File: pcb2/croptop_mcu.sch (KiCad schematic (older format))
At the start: 63 parts, among them J1 USB-A1HSW6, J2 USB-A1HSW6, J3 68000-206HLF, SW1 SW_Push, U1 TPD4E1U06, U2 FSUSB42, U3 AP22802AW5, U4 AP22802AW5, U5 74AUP2G57, U6 PIC32MX795F512L, Y1 ABLS-8.000MHZ-B4-T

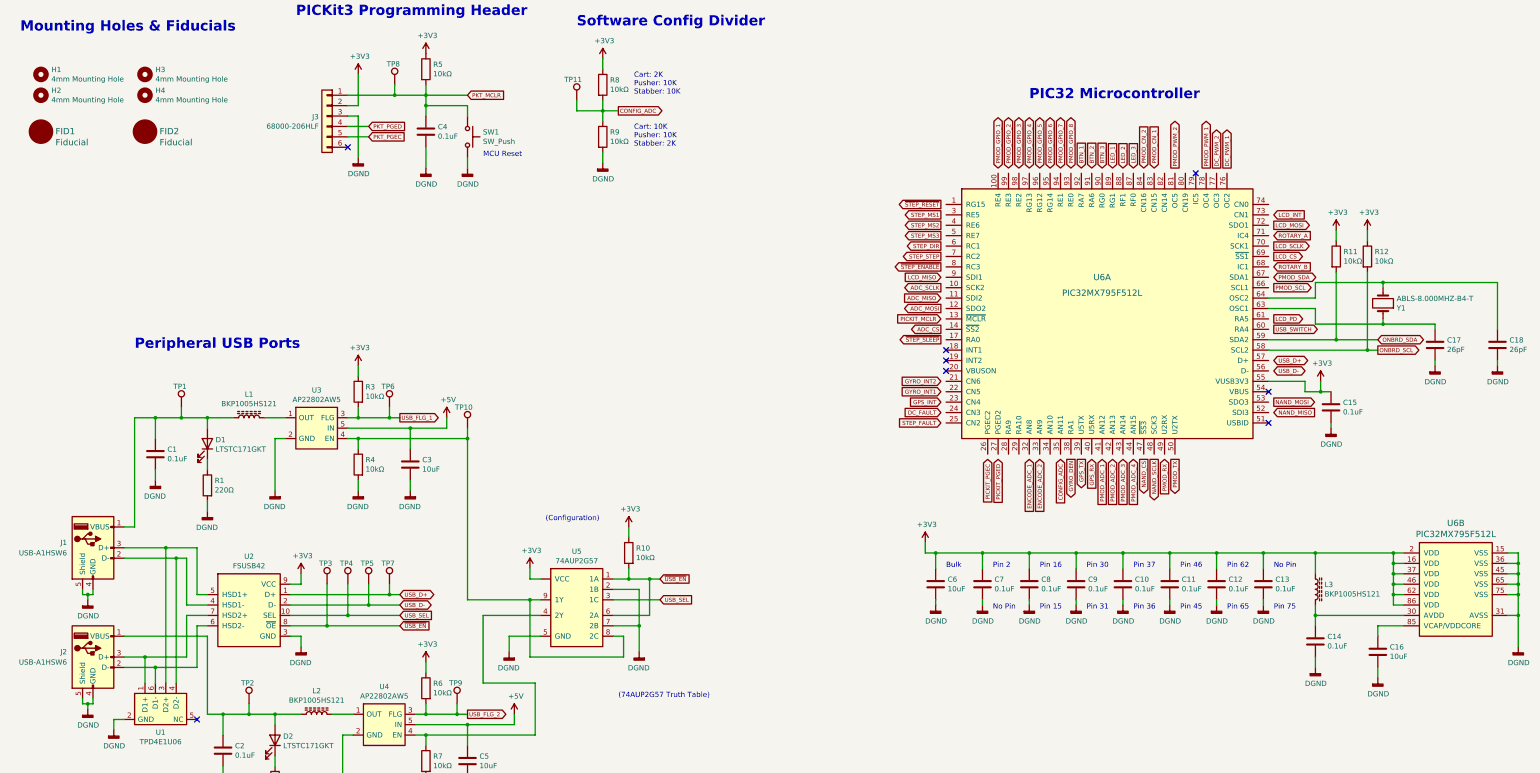
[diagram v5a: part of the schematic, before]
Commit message: Added TVS diodes
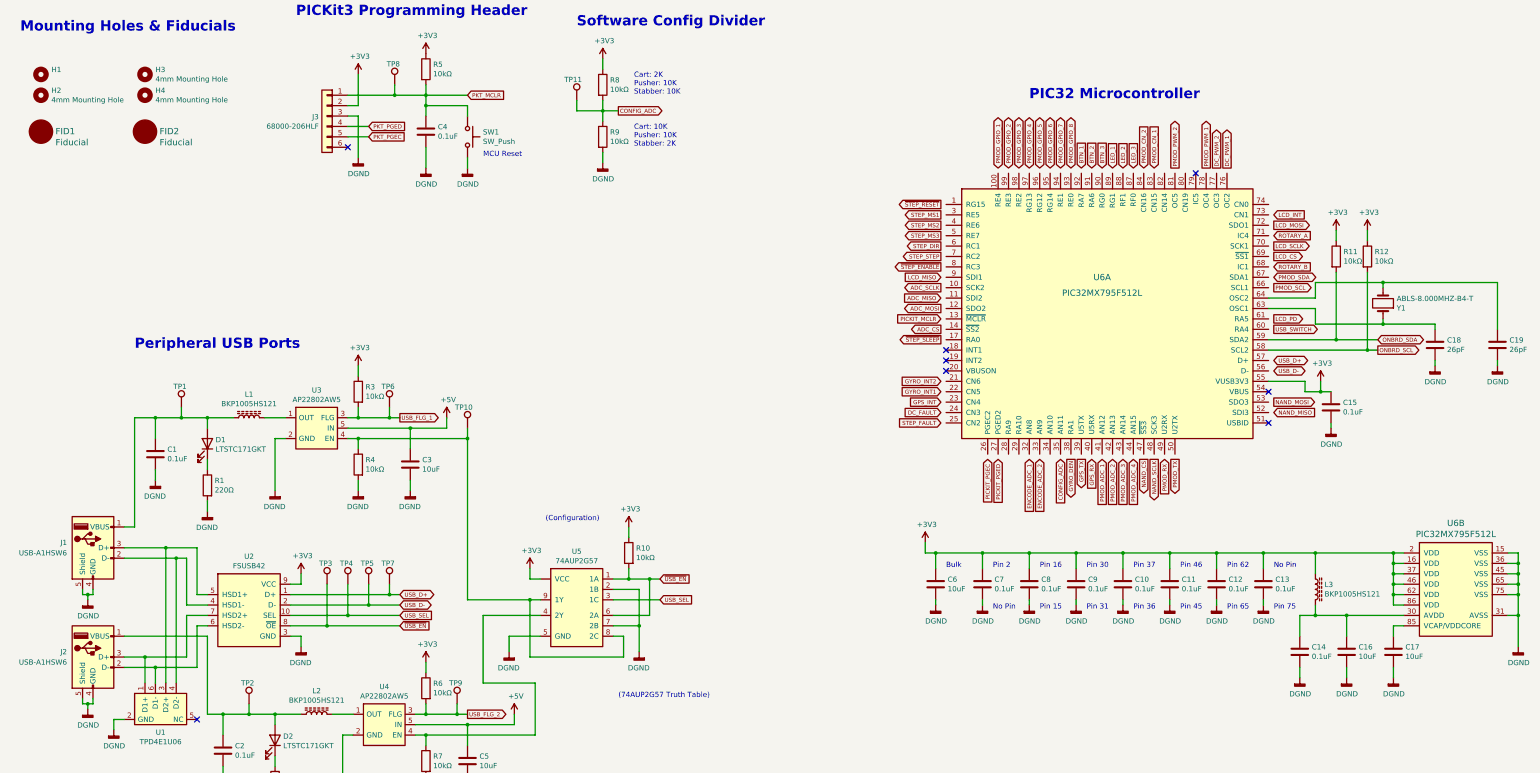
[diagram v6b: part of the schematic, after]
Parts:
- added C16: 10uF, Capacitor_SMD:C_0402_1005Metric, symbol Device:C
- renumbered C16 to C17, C17 to C18, C18 to C19
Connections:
- net DGND: now also C16.2
- net at C14.1, L3.2, U6.30 (AVDD): now also C16.1
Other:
- moved on the sheet: C14, C17
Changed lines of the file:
@@
 P 1200 1800
 F 0 "H1" H 1300 1846 50  0000 L CNN
-F 1 "4mm Mounting Hole" H 1300 1755 50  0000 L CNN
+F 1 "4mm Mounting Hole" H 1300 1755 50  0001 L CNN
 F 2 "MountingHole:MountingHole_4mm_Pad" H 1200 1800 50  0001 C CNN
 F 3 "" H 1200 1800 50  0001 C CNN
@@
 	14100 3800 14100 3850
 $Comp
-L CropTop:DGND #PWR047
+L CropTop:DGND #PWR048
 U 1 1 5D1D7CEB
 P 15200 4600
-F 0 "#PWR047" H 15200 4350 50  0001 C CNN
+F 0 "#PWR048" H 15200 4350 50  0001 C CNN
 F 1 "DGND" H 15204 4445 50  0000 C CNN
 F 2 "" H 15200 4600 50  0001 C CNN
@@
 $EndComp
 $Comp
-L CropTop:DGND #PWR046
+L CropTop:DGND #PWR047
 U 1 1 5D1D7CF1
 P 14600 4600
-F 0 "#PWR046" H 14600 4350 50  0001 C CNN
+F 0 "#PWR047" H 14600 4350 50  0001 C CNN
 F 1 "DGND" H 14604 4445 50  0000 C CNN
 F 2 "" H 14600 4600 50  0001 C CNN
@@
 P 15200 4400
 AR Path="/5D1D7CFB" Ref="C?"  Part="1"
-AR Path="/64807BBC/5D1D7CFB" Ref="C18"  Part="1"
-F 0 "C18" H 15315 4446 50  0000 L CNN
+AR Path="/64807BBC/5D1D7CFB" Ref="C19"  Part="1"
+F 0 "C19" H 15315 4446 50  0000 L CNN
 F 1 "26pF" H 15315 4355 50  0000 L CNN
 F 2 "Capacitor_SMD:C_0402_1005Metric" H 15238 4250 50  0001 C CNN
@@
 P 14600 4400
 AR Path="/5D1D7D02" Ref="C?"  Part="1"
-AR Path="/64807BBC/5D1D7D02" Ref="C17"  Part="1"
-F 0 "C17" H 14715 4446 50  0000 L CNN
+AR Path="/64807BBC/5D1D7D02" Ref="C18"  Part="1"
+F 0 "C18" H 14715 4446 50  0000 L CNN
 F 1 "26pF" H 14715 4355 50  0000 L CNN
 F 2 "Capacitor_SMD:C_0402_1005Metric" H 14638 4250 50  0001 C CNN
@@
 	14200 6400 14300 6400
 $Comp
-L CropTop:DGND #PWR048
+L CropTop:DGND #PWR049
 U 1 1 5D8970DB
 P 15400 7300
-F 0 "#PWR048" H 15400 7050 50  0001 C CNN
+F 0 "#PWR049" H 15400 7050 50  0001 C CNN
 F 1 "DGND" H 15404 7145 50  0000 C CNN
 F 2 "" H 15400 7300 50  0001 C CNN
@@
 	15400 6500 15400 6600
 $Comp
-L Device:C C16
+L Device:C C17
 U 1 1 5D939999
-P 14050 7350
-F 0 "C16" H 14165 7396 50  0000 L CNN
-F 1 "10uF" H 14165 7305 50  0000 L CNN
-F 2 "Capacitor_SMD:C_0402_1005Metric" H 14088 7200 50  0001 C CNN
-F 3 "" H 14050 7350 50  0001 C CNN
-	1    14050 7350
+P 14200 7350
+F 0 "C17" H 14315 7396 50  0000 L CNN
+F 1 "10uF" H 14315 7305 50  0000 L CNN
+F 2 "Capacitor_SMD:C_0402_1005Metric" H 14238 7200 50  0001 C CNN
+F 3 "" H 14200 7350 50  0001 C CNN
+	1    14200 7350
 	1    0    0    -1
 $EndComp
@@
 	1    0    0    -1
 $EndComp
-$Comp
-L CropTop:DGND #PWR03
-U 1 1 6104C614
-P 1900 8100
-AR Path="/64807BBC/6104C614" Ref="#PWR03"  Part="1"
-AR Path="/669AB112/6104C614" Ref="#PWR?"  Part="1"
-F 0 "#PWR03" H 1900 7850 50  0001 C CNN
-F 1 "DGND" H 1904 7945 50  0000 C CNN
-F 2 "" H 1900 8100 50  0001 C CNN
-F 3 "" H 1900 8100 50  0001 C CNN
-	1    1900 8100
-	1    0    0    -1
-$EndComp
-Wire Wire Line
-	2000 8000 1900 8000
-Wire Wire Line
-	1900 8000 1900 8100
 NoConn ~ 2700 8000
 NoConn ~ 13000 4850
@@
 Wire Wire Line
 	3700 7200 3700 7300
-$Comp
-L CropTop:TPD4E1U06 U?
-U 1 1 60F8235A
-P 2350 7900
-AR Path="/669AB112/60F8235A" Ref="U?"  Part="1"
-AR Path="/64807BBC/60F8235A" Ref="U1"  Part="1"
-F 0 "U1" H 2350 7676 50  0000 C CNN
-F 1 "TPD4E1U06" H 2350 7585 50  0000 C CNN
-F 2 "" V 2600 7350 50  0001 C CNN
-F 3 "" V 2600 7350 50  0001 C CNN
-	1    2350 7900
-	1    0    0    -1
-$EndComp
 Wire Wire Line
 	2600 7000 2600 7400
@@
 $EndComp
 $Comp
-L power:+3V3 #PWR044
+L power:+3V3 #PWR045
 U 1 1 5CF40AEC
 P 13950 3300
-F 0 "#PWR044" H 13950 3150 50  0001 C CNN
+F 0 "#PWR045" H 13950 3150 50  0001 C CNN
 F 1 "+3V3" H 13965 3473 50  0000 C CNN
 F 2 "" H 13950 3300 50  0001 C CNN
@@
 L Device:C C?
 U 1 1 5D054B37
-P 13450 7250
+P 13300 7350
 AR Path="/5D054B37" Ref="C?"  Part="1"
 AR Path="/66A12209/5D054B37" Ref="C?"  Part="1"
 AR Path="/64807BBC/5D054B37" Ref="C14"  Part="1"
-F 0 "C14" H 13565 7296 50  0000 L CNN
-F 1 "0.1uF" H 13565 7205 50  0000 L CNN
-F 2 "Capacitor_SMD:C_0402_1005Metric" H 13488 7100 50  0001 C CNN
-F 3 "" H 13450 7250 50  0001 C CNN
-	1    13450 7250
-	1    0    0    -1
-$EndComp
-$Comp
-L CropTop:DGND #PWR045
+F 0 "C14" H 13415 7396 50  0000 L CNN
+F 1 "0.1uF" H 13415 7305 50  0000 L CNN
+F 2 "Capacitor_SMD:C_0402_1005Metric" H 13338 7200 50  0001 C CNN
+F 3 "" H 13300 7350 50  0001 C CNN
+	1    13300 7350
+	1    0    0    -1
+$EndComp
+$Comp
+L CropTop:DGND #PWR046
 U 1 1 5D0824AF
-P 14050 7600
-F 0 "#PWR045" H 14050 7350 50  0001 C CNN
-F 1 "DGND" H 14054 7445 50  0000 C CNN
-F 2 "" H 14050 7600 50  0001 C CNN
-F 3 "" H 14050 7600 50  0001 C CNN
-	1    14050 7600
-	1    0    0    -1
-$EndComp
-Wire Wire Line
-	14050 7500 14050 7600
+P 14200 7600
+F 0 "#PWR046" H 14200 7350 50  0001 C CNN
+F 1 "DGND" H 14204 7445 50  0000 C CNN
+F 2 "" H 14200 7600 50  0001 C CNN
+F 3 "" H 14200 7600 50  0001 C CNN
+	1    14200 7600
+	1    0    0    -1
+$EndComp
+Wire Wire Line
+	14200 7500 14200 7600
 $Comp
 L CropTop:DGND #PWR040
 U 1 1 5D091954
-P 13450 7500
-F 0 "#PWR040" H 13450 7250 50  0001 C CNN
-F 1 "DGND" H 13454 7345 50  0000 C CNN
-F 2 "" H 13450 7500 50  0001 C CNN
-F 3 "" H 13450 7500 50  0001 C CNN
-	1    13450 7500
-	1    0    0    -1
-$EndComp
-Wire Wire Line
-	13450 7400 13450 7500
+P 13300 7600
+F 0 "#PWR040" H 13300 7350 50  0001 C CNN
+F 1 "DGND" H 13304 7445 50  0000 C CNN
+F 2 "" H 13300 7600 50  0001 C CNN
+F 3 "" H 13300 7600 50  0001 C CNN
+	1    13300 7600
+	1    0    0    -1
+$EndComp
+Wire Wire Line
+	13300 7500 13300 7600
 Wire Wire Line
 	12950 6400 13450 6400
@@
 	13450 6400 13450 6600
 Wire Wire Line
-	14050 7200 14050 7100
-Wire Wire Line
-	14050 7100 14300 7100
+	14200 7200 14200 7100
 Wire Wire Line
 	13450 6900 13450 7000
@@
 	13450 6400 14200 6400
 Connection ~ 13450 6400
-Wire Wire Line
-	13450 7000 14300 7000
-Connection ~ 13450 7000
-Wire Wire Line
-	13450 7000 13450 7100
 Connection ~ 2950 7950
 Connection ~ 3450 7950
@@
 Wire Wire Line
 	5950 7650 5950 8150
+$Comp
+L CropTop:TPD4E1U06 U?
+U 1 1 60F8235A
+P 2350 7900
+AR Path="/669AB112/60F8235A" Ref="U?"  Part="1"
+AR Path="/64807BBC/60F8235A" Ref="U1"  Part="1"
+F 0 "U1" H 2350 7676 50  0000 C CNN
+F 1 "TPD4E1U06" H 2350 7585 50  0000 C CNN
+F 2 "" V 2600 7350 50  0001 C CNN
+F 3 "" V 2600 7350 50  0001 C CNN
+	1    2350 7900
+	1    0    0    -1
+$EndComp
+Wire Wire Line
+	1900 8000 1900 8100
+Wire Wire Line
+	2000 8000 1900 8000
+$Comp
+L CropTop:DGND #PWR03
+U 1 1 6104C614
+P 1900 8100
+AR Path="/64807BBC/6104C614" Ref="#PWR03"  Part="1"
+AR Path="/669AB112/6104C614" Ref="#PWR?"  Part="1"
+F 0 "#PWR03" H 1900 7850 50  0001 C CNN
+F 1 "DGND" H 1904 7945 50  0000 C CNN
+F 2 "" H 1900 8100 50  0001 C CNN
+F 3 "" H 1900 8100 50  0001 C CNN
+	1    1900 8100
+	1    0    0    -1
+$EndComp
+$Comp
+L Device:C C16
+U 1 1 5DDFE105
+P 13750 7350
+F 0 "C16" H 13865 7396 50  0000 L CNN
+F 1 "10uF" H 13865 7305 50  0000 L CNN
+F 2 "Capacitor_SMD:C_0402_1005Metric" H 13788 7200 50  0001 C CNN
+F 3 "" H 13750 7350 50  0001 C CNN
+	1    13750 7350
+	1    0    0    -1
+$EndComp
+$Comp
+L CropTop:DGND #PWR044
+U 1 1 5DDFE10C
+P 13750 7600
+F 0 "#PWR044" H 13750 7350 50  0001 C CNN
+F 1 "DGND" H 13754 7445 50  0000 C CNN
+F 2 "" H 13750 7600 50  0001 C CNN
+F 3 "" H 13750 7600 50  0001 C CNN
+	1    13750 7600
+	1    0    0    -1
+$EndComp
+Wire Wire Line
+	13750 7500 13750 7600
+Wire Wire Line
+	14200 7100 14300 7100
+Wire Wire Line
+	13300 7000 13450 7000
+Wire Wire Line
+	13300 7000 13300 7200
+Connection ~ 13450 7000
+Wire Wire Line
+	13750 7200 13750 7000
+Wire Wire Line
+	13450 7000 13750 7000
+Connection ~ 13750 7000
+Wire Wire Line
+	13750 7000 14300 7000
 $EndSCHEMATC

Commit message: Updated pin out
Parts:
- removed C1, C10, C11, C12, C13, C14, C15, C2, C4, C7, C8, C9: 0.1uF, Capacitor_SMD:C_0402_1005Metric, symbol Device:C
- removed C16, C17, C3, C5, C6: 10uF, Capacitor_SMD:C_0402_1005Metric, symbol Device:C
- removed C18, C19: 26pF, Capacitor_SMD:C_0402_1005Metric, symbol Device:C
- removed D1, D2: LTSTC171GKT, LED_SMD:LED_0805_2012Metric, symbol Device:LED
- removed FID1, FID2: Fiducial, Fiducial:Fiducial_1mm_Dia_2.54mm_Outer_CopperTop, symbol CropTop:FIDUCIAL
- removed H1, H2, H3, H4: 4mm Mounting Hole, MountingHole:MountingHole_4mm_Pad, symbol Mechanical:MountingHole
- removed J1, J2: USB-A1HSW6, croptop:USB_A_Assmann_Horizontal, symbol Connector:USB_A
- removed J3: 68000-206HLF, symbol Connector_Generic:Conn_01x06
- removed L1, L2, L3: BKP1005HS121, symbol Device:L_Core_Ferrite
- removed R1, R2: 220Ω, Resistor_SMD:R_0402_1005Metric, symbol Device:R
- removed R10, R11, R12, R3, R4, R5, R6, R7, R8, R9: 10kΩ, Resistor_SMD:R_0402_1005Metric, symbol Device:R
- removed SW1: SW_Push, symbol Switch:SW_Push
- removed TP1, TP10, TP11, TP2, TP3, TP4, TP5, TP6, TP7, TP8, TP9: TestPoint, symbol Connector:TestPoint
- removed U1: TPD4E1U06, symbol CropTop:TPD4E1U06
- removed U2: FSUSB42, symbol CropTop:FSUSB42
- removed U3, U4: AP22802AW5, symbol CropTop:AP22802AW5
- removed U5: 74AUP2G57, symbol CropTop:74AUP2G57
- removed U6: PIC32MX795F512L, digikey-footprints:TQFP-100_12x12mm, symbol CropTop:PIC32MX795F512L-80I_PT_0
- removed Y1: ABLS-8.000MHZ-B4-T, croptop:ABLS_OX, symbol Device:Crystal
- added C? (x3): 100uF, Capacitor_SMD:CP_Elec_6.3x7.7, symbol Device:CP1
- added C? (x14): 0.1uF, Capacitor_SMD:C_0402_1005Metric, symbol Device:C
- added C? (x14): 10uF, Capacitor_SMD:C_0402_1005Metric, symbol Device:C
- added C? (x2): 26pF, Capacitor_SMD:C_0402_1005Metric, symbol Device:C
- added D?: NSR0240HT1G, croptop:D_SOD-123, symbol Device:D_Schottky
- added D? (x5): LTSTC171GKT, LED_SMD:LED_0805_2012Metric, symbol Device:LED
- added D?: TPD1E6B06, symbol Device:D_TVS
- added FID? (x2): Fiducial, Fiducial:Fiducial_1mm_Dia_2.54mm_Outer_CopperTop, symbol CropTop:FIDUCIAL
- added H? (x4): 4mm Mounting Hole, MountingHole:MountingHole_4mm_Pad, symbol Mechanical:MountingHole
- added J?: 10118193-0001LF, croptop:USB_Micro-B_Molex_47346-0001, symbol Connector:USB_B_Micro
- added J?: 68000-206HLF, symbol Connector_Generic:Conn_01x06
- added J?: USB-A1HSW6, croptop:USB_A_Assmann_Horizontal, symbol Connector:USB_A
- added L?: 2.2uH, symbol Device:L
- added L?: 4.7uH, Inductor_SMD:L_1210_3225Metric, symbol Device:L
- added L?: BKP1005HS121, symbol Device:L_Core_Ferrite
- added R?: 1.1, Resistor_SMD:R_0402_1005Metric, symbol Device:R
- added R? (x5): 220, Resistor_SMD:R_0402_1005Metric, symbol Device:R
- added R? (x2): 100, Resistor_SMD:R_0402_1005Metric, symbol Device:R
- added R?: 0, Resistor_SMD:R_0402_1005Metric, symbol Device:R
- added R? (x8): 10k, Resistor_SMD:R_0402_1005Metric, symbol Device:R
- added SW?: SW_Push, symbol Switch:SW_Push
- added TP? (x11): TestPoint, symbol Connector:TestPoint
- added U?: REG71055, Package_TO_SOT_SMD:SOT-23-6, symbol CropTop:REG71055
- added U?: TPS62131, Package_DFN_QFN:QFN-16-1EP_3x3mm_P0.5mm_EP1.8x1.8mm, symbol CropTop:TPS62131
- added U?: TPS61169, symbol CropTop:TPS61169
- added U?: TPS70950, symbol CropTop:TPS70950
- added U?: TPD4E1U06, symbol CropTop:TPD4E1U06
- added U?: AP22802AW5, symbol CropTop:AP22802AW5
- added U? (x2): PIC32MX795F512L, digikey-footprints:TQFP-100_12x12mm, symbol CropTop:PIC32MX795F512L
- added Y?: ABLS-8.000MHZ-B4-T, croptop:ABLS_OX, symbol Device:Crystal
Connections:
- net +3V3: now also C?.1, C?.1, C?.1, C?.1, C?.1, C?.1, C?.1, C?.1, C?.1, C?.1, C?.1, D?.2 (A), J?.2 (Pin_2), L?.1, L?.1, R?.1, R?.1, R?.1, R?.1, R?.1, TP?.1, U?.14 (VOS), U?.16 (VDD), U?.2 (VDD), U?.37 (VDD), U?.4 (EN), U?.46 (VDD), U?.62 (VDD), U?.86 (VDD)
- net +5V: now also C?.1, C?.1, C?.1, C?.1, C?.1, D?.1 (A1), D?.2 (A), J?.1 (VBUS), L?.2, TP?.1, U?.10 (AVIN), U?.11 (PVIN), U?.12 (PVIN), U?.13 (EN), U?.3 (EN), U?.5 (VIN), U?.5 (VIN)
- net CONFIG_ADC: now also R?.1, R?.2, TP?.1
- net DGND: now also C?.2, C?.2, C?.2, C?.2, C?.2, C?.2, C?.2, C?.2, C?.2, C?.2, C?.2, C?.2, C?.2, C?.2, C?.2, C?.2, C?.2, C?.2, C?.2, C?.2, C?.2, C?.2, C?.2, C?.2, C?.2, C?.2, C?.2, C?.2, C?.2, D?.2 (A2), J?.3 (Pin_3), J?.4 (GND), J?.5 (GND), J?.5 (Shield), J?.6 (Shield), R?.1, R?.2, R?.2, R?.2, R?.2, R?.2, R?.2, R?.2, R?.2, SW?.2, U?.15 (PGND), U?.15 (VSS), U?.16 (PGND), U?.17 (EP), U?.2 (GND), U?.2 (GND), U?.2 (GND), U?.2 (GND), U?.31 (AVSS), U?.36 (VSS), U?.4 (PG), U?.45 (VSS), U?.5 (FB), U?.6 (AGND), U?.65 (VSS), U?.7 (FSW), U?.75 (VSS), U?.8 (DEF)
- net PKT_MCLR: now also C?.1, J?.1 (Pin_1), R?.2, SW?.1, TP?.1
- net PKT_PGEC: now also J?.5 (Pin_5)
- net PKT_PGED: now also J?.4 (Pin_4)
- new net: C?.1, C?.1, TP?.1, U?.1 (VIN), U?.1 (VOUT), U?.3 (EN)
- new net: C?.2, U?.4 (C-)
- new net: C?.1, U?.6 (C+)
- new net: L?.2, U?.1 (SW), U?.2 (SW), U?.3 (SW)
- new net: D?.2 (A), L?.1, U?.1 (SW)
- new net: D?.1 (K), R?.1 (x5)
- new net: R?.1, R?.2 (x2)
- new net: C?.1, U?.9 (SS/TR)
- new net: C?.1, U?.85 (VCAP/VDDCORE)
- new net: C?.1, C?.1, L?.2, U?.30 (AVDD)
- new net: C?.1, C?.1, D?.2 (A), J?.1 (VBUS), TP?.1, U?.1 (OUT)
- new net: J?.2 (D-), U?.3 (D2+)
- new net: J?.3 (D+), U?.4 (D2-)
- new net: C?.1, U?.5 (IN)
- new net: R?.2, TP?.1, U?.3 (FLG)
- new net +5V_REG: C?.1, C?.1, D?.2 (A), TP?.1, U?.5 (VOUT)
- new net AGND: C?.2, C?.2, C?.2, R?.2, R?.2, U?.2 (GND)
- new net GCD_PWM: R?.1, TP?.1, U?.4 (CNTL)
- new net LCD_A: C?.1, D?.1 (K), D?.2 (A), TP?.1
- new net LCD_K: C?.1, R?.1, TP?.1, U?.3 (FB)
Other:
- note added: "(50ms Soft Start)"
- note added: "(approx. 9.6V)"
- note added: "DGND & AGND\nStar Ground"
- note added: "Digital & Analog Power Supply"
- note added: "Individual LEDs:\n3.2V Forward Voltage\n20mA Typical / 25mA Max\n\nTotal:\n9.6V Forward Voltage\n180mA Typical / 225mA Max"
- note added: "Low Noise 5V Plane"
- note added: "RC1005F1R1CS"
- note added: "SRN6045TA-4R7M"
- note added: "SRN8040-2R2Y"
- note added: "USB 2.0 Host Interface"
- note removed: "(74AUP2G57 Truth Table)"
- note removed: "(Configuration)"
- note removed: "Peripheral USB Ports"

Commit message: Final Schematic
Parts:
- removed R?: 0, Resistor_SMD:R_0402_1005Metric, symbol Device:R
- added R? (x2): 10k, Resistor_SMD:R_0402_1005Metric, symbol Device:R
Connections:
- net AGND is gone; now on net DGND: C?.2, C?.2, C?.2, R?.2, U?.2 (GND)
- net +3V3: now also C?.1, R?.1, U?.5 (IN), R?.1, R?.1; no longer R?.1, U?.4 (EN)
- net USB_D+: now also J?.3 (D+), U?.4 (D2-)
- net USB_D-: now also J?.2 (D-), U?.3 (D2+)
- net at U?.63 (OSC1): now also C?.1, Y?.1
- net at U?.64 (OSC2): now also C?.1, Y?.2
- net GCD_PWM renamed GPU_PWM
- new net: R?.1, U?.4 (EN)
- no-connect marks 8 -> 10
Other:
- note added: "Ensure return currents are local"
- note removed: "DGND & AGND\nStar Ground"
- note removed: "Low Noise 5V Plane"
- moved on the sheet: C?, D?, J?, R?, TP?, U?, U?A, Y?
